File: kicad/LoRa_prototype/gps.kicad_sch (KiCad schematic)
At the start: 15 parts, among them Q1 DTC143Z, Q2 DTC143Z, U6 L80-R

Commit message: Done schematic for GPS and gas sensors (Milestone)
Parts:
- added C41: 10uF, symbol Device:C
- added TP18: BMV_GND, symbol Connector:TestPoint
- added TP19: BMV_VDD, symbol Connector:TestPoint
- added U7: BME688, BME688:IC_BME688, symbol BME688:BME688
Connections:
- net GND: now also BMV080.11 (MISO), BMV080.4 (CSB), C41.2, TP18.1, U7.1 (GND), U7.5 (SDO), U7.7 (GND)
- net VDD: now also C41.1, TP19.1, U7.2 (CSB), U7.6 (VDDIO), U7.8 (VDD)
- new net SCL_BME: U7.4 (SCK)
- new net SDA_BME: U7.3 (SDI)
- no-connect marks 7 -> 5
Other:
- note added: "(1.2-3.3V)"
- note added: "(2.5-3.3V)"
- note added: "(I2C_ADDR=0x54)"
- note added: "(I2C_ADDR=0x76)"
- note added: "(pullup on MCU side)"
- note added: "BME688"
- note added: "BMV080"
- note added: "GAS SENSORS"
- note added: "GPS MODULE"
- title: (none) -> GPS and gas sensor modules
- moved on the sheet: BMV080, C38, C39, C40, D2, Q1, Q2, R19, R20, R21, R22, TP15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

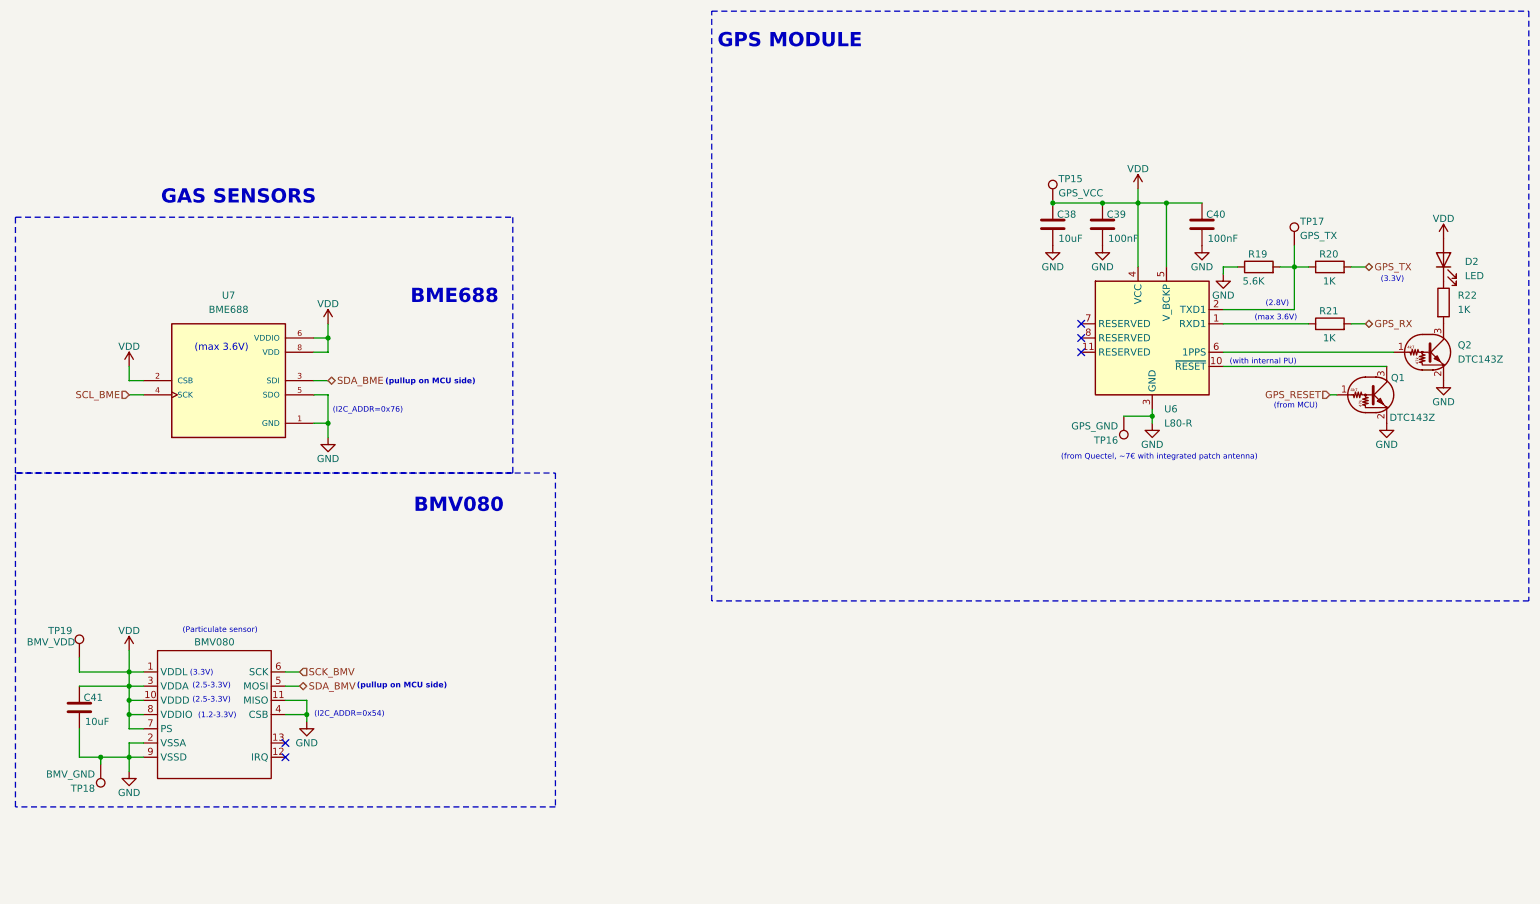
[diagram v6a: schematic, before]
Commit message: Added pin headers in schematics
To activate/deactivate subsystems as well as measure currents
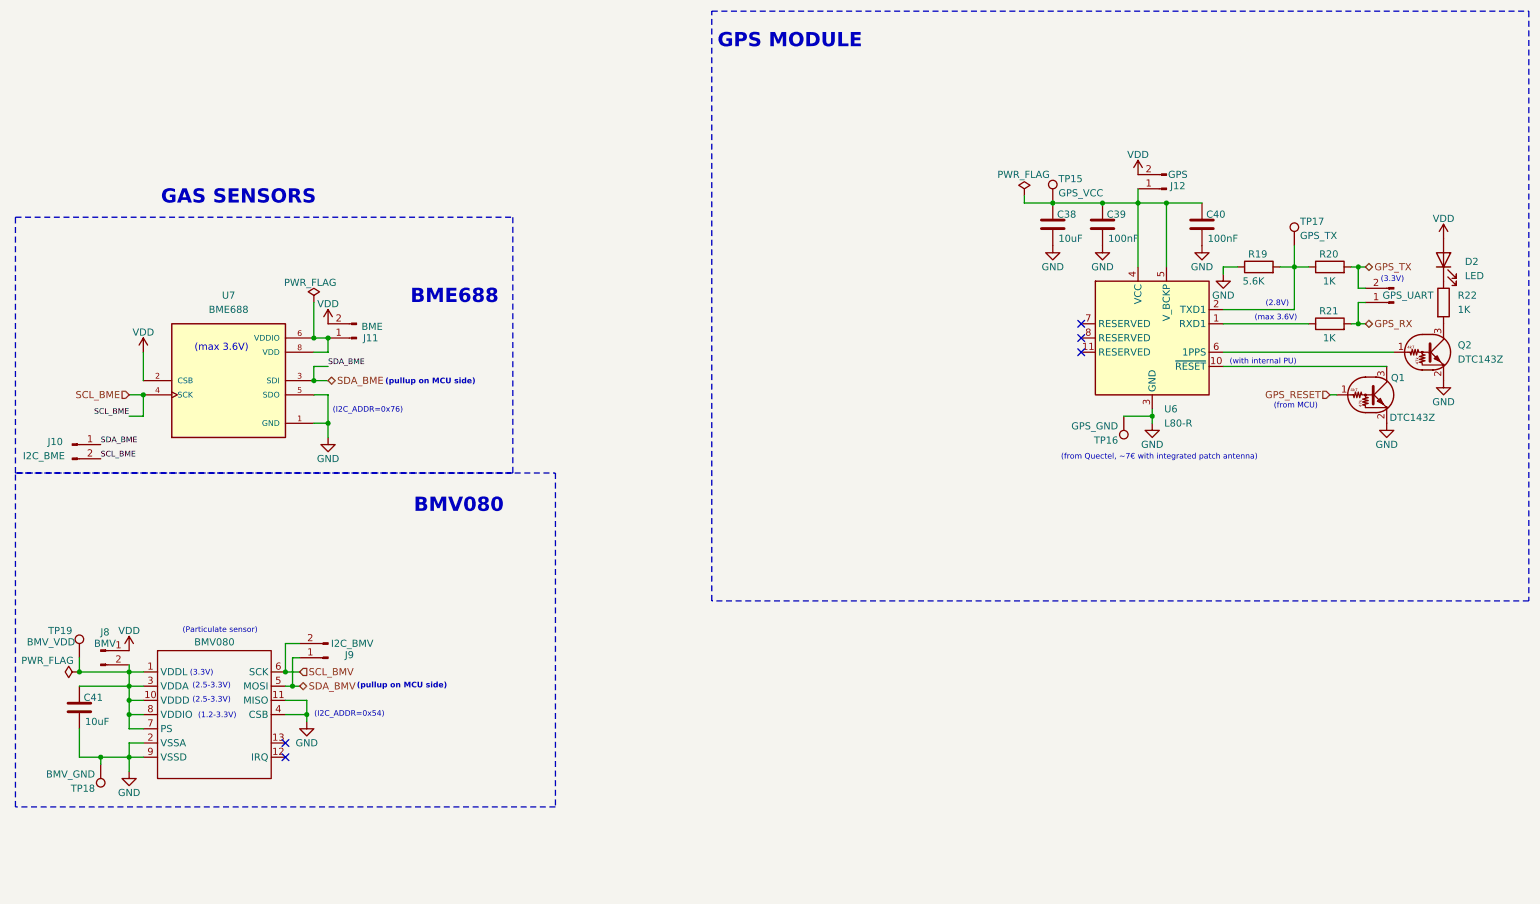
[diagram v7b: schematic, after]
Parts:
- added J10: I2C_BME, Connector_PinHeader_2.54mm:PinHeader_1x02_P2.54mm_Vertical, symbol Connector:Conn_01x02_Pin
- added J11: BME, Connector_PinHeader_2.54mm:PinHeader_1x02_P2.54mm_Vertical, symbol Connector:Conn_01x02_Pin
- added J12: GPS, Connector_PinHeader_2.54mm:PinHeader_1x02_P2.54mm_Vertical, symbol Connector:Conn_01x02_Pin
- added J13: GPS_UART, Connector_PinHeader_2.54mm:PinHeader_1x02_P2.54mm_Vertical, symbol Connector:Conn_01x02_Pin
- added J8: BMV, Connector_PinHeader_2.54mm:PinHeader_1x02_P2.54mm_Vertical, symbol Connector:Conn_01x02_Pin
- added J9: I2C_BMV, Connector_PinHeader_2.54mm:PinHeader_1x02_P2.54mm_Vertical, symbol Connector:Conn_01x02_Pin
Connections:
- net GPS_RX: now also J13.1 (Pin_1)
- net GPS_TX: now also J13.2 (Pin_2)
- net SCL_BME: now also J10.2 (Pin_2)
- net SDA_BME: now also J10.1 (Pin_1)
- net SDA_BMV: now also J9.1 (Pin_1)
- net VDD: now also J11.2 (Pin_2), J12.2 (Pin_2), J8.1 (Pin_1); no longer BMV080.1 (VDDL), BMV080.10 (VDDD), BMV080.3 (VDDA), BMV080.7 (PS), BMV080.8 (VDDIO), C38.1, C39.1, C40.1, C41.1, TP15.1, TP19.1, U6.4 (VCC), U6.5 (V_BCKP), U7.6 (VDDIO), U7.8 (VDD)
- net SCK_BMV renamed SCL_BMV
- net SCL_BMV: now also J9.2 (Pin_2)
- new net: C38.1, C39.1, C40.1, J12.1 (Pin_1), TP15.1, U6.4 (VCC), U6.5 (V_BCKP)
- new net: J11.1 (Pin_1), U7.6 (VDDIO), U7.8 (VDD)
- new net: BMV080.1 (VDDL), BMV080.10 (VDDD), BMV080.3 (VDDA), BMV080.7 (PS), BMV080.8 (VDDIO), C41.1, J8.2 (Pin_2), TP19.1

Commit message: Created separate folders for footprints and 3d models
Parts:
- BMV080: footprint (none) -> footprints:CON_5035661302_MOL
- C38, C39, C40, C41: footprint (none) -> Capacitor_SMD:C_0805_2012Metric
- D2: footprint (none) -> LED_SMD:LED_0805_2012Metric
- Q1, Q2: footprint (none) -> footprints:SOTFL50P160X85-3N
- R19, R20, R21, R22: footprint (none) -> Resistor_SMD:R_0805_2012Metric
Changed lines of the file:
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@@
 			)
 		)
-		(property "Footprint" ""
+		(property "Footprint" "LED_SMD:LED_0805_2012Metric"
 			(at 269.24 57.15 0)
 			(effects
@@
 			)
 		)
-		(property "Footprint" ""
+		(property "Footprint" "footprints:SOTFL50P160X85-3N"
 			(at 256.54 81.28 0)
 			(effects
@@
 			)
 		)
-		(property "Footprint" ""
+		(property "Footprint" "Resistor_SMD:R_0805_2012Metric"
 			(at 267.462 64.77 90)
 			(effects
@@
 			)
 		)
-		(property "Footprint" ""
+		(property "Footprint" "Capacitor_SMD:C_0805_2012Metric"
 			(at 209.2452 54.61 0)
 			(effects
@@
 			)
 		)
-		(property "Footprint" ""
+		(property "Footprint" "Resistor_SMD:R_0805_2012Metric"
 			(at 248.92 60.198 90)
 			(effects
@@
 			)
 		)
-		(property "Footprint" ""
+		(property "Footprint" "Capacitor_SMD:C_0805_2012Metric"
 			(at 227.0252 54.61 0)
 			(effects
@@
 			)
 		)
-		(property "Footprint" ""
+		(property "Footprint" "Resistor_SMD:R_0805_2012Metric"
 			(at 248.92 70.358 90)
 			(effects
@@
 			)
 		)
-		(property "Footprint" ""
+		(property "Footprint" "footprints:CON_5035661302_MOL"
 			(at 44.45 137.16 0)
 			(effects
@@
 			)
 		)
-		(property "Footprint" ""
+		(property "Footprint" "footprints:SOTFL50P160X85-3N"
 			(at 266.7 73.66 0)
 			(effects
@@
 			)
 		)
-		(property "Footprint" ""
+		(property "Footprint" "Resistor_SMD:R_0805_2012Metric"
 			(at 236.22 60.198 90)
 			(effects
@@
 			)
 		)
-		(property "Footprint" ""
+		(property "Footprint" "Capacitor_SMD:C_0805_2012Metric"
 			(at 200.3552 54.61 0)
 			(effects
@@
 			)
 		)
-		(property "Footprint" ""
+		(property "Footprint" "Capacitor_SMD:C_0805_2012Metric"
 			(at 26.3652 140.97 0)
 			(effects
